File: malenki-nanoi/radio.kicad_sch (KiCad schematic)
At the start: 22 parts, among them U1 A7105, Y1 16 Mhz 20ppm

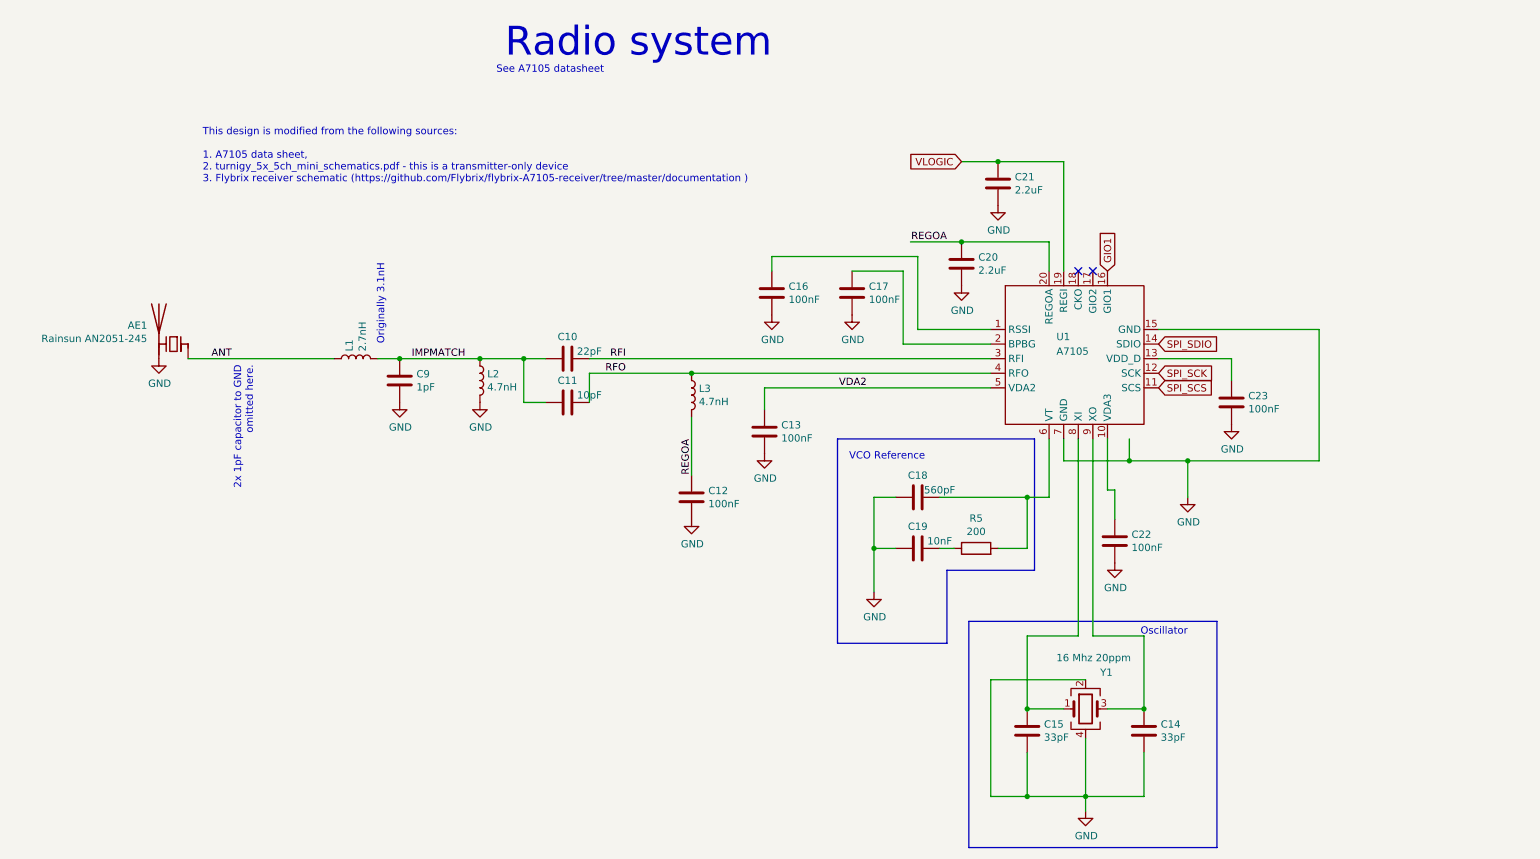
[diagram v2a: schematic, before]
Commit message: 4-layer Malenki-nano
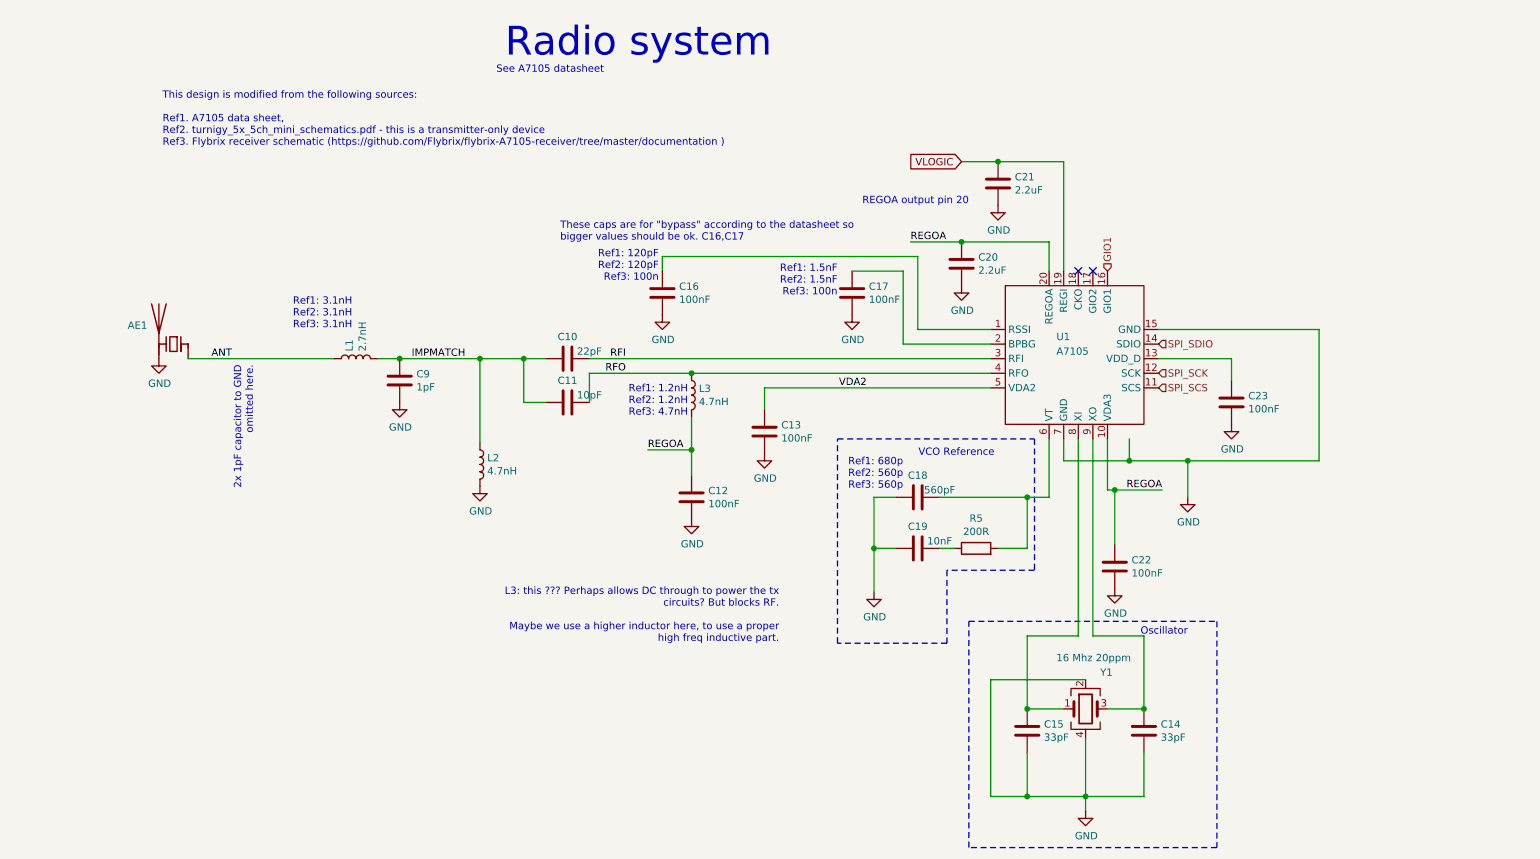
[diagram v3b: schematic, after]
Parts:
- AE1: value Rainsun AN2051-245 -> ~; footprint RF_Antenna:Johanson_2450AT43F0100 -> RF_Antenna:Texas_SWRA117D_2.4GHz_Left; LCSC C99727 -> (none)
- C10: footprint Capacitor_SMD:C_0603_1608Metric -> Capacitor_SMD:C_0402_1005Metric; LCSC C1653 -> (none)
- C11: footprint Capacitor_SMD:C_0603_1608Metric -> Capacitor_SMD:C_0402_1005Metric; LCSC C1634 -> (none)
- C12, C13, C16, C17, C22, C23: footprint Capacitor_SMD:C_0603_1608Metric -> Capacitor_SMD:C_0402_1005Metric; LCSC C14663 -> (none)
- C14, C15: footprint Capacitor_SMD:C_0603_1608Metric -> Capacitor_SMD:C_0402_1005Metric; LCSC C1663 -> (none)
- C18: footprint Capacitor_SMD:C_0603_1608Metric -> Capacitor_SMD:C_0402_1005Metric; LCSC C84721 -> (none)
- C19: footprint Capacitor_SMD:C_0603_1608Metric -> Capacitor_SMD:C_0402_1005Metric; LCSC C57112 -> (none)
- C20, C21: LCSC C23630 -> (none)
- C9: footprint Capacitor_SMD:C_0603_1608Metric -> Capacitor_SMD:C_0402_1005Metric; LCSC C23969 -> (none)
- L1, L2, L3: footprint Inductor_SMD:L_0603_1608Metric -> Inductor_SMD:L_0402_1005Metric
- R5: value 200 -> 200R; footprint Resistor_SMD:R_0603_1608Metric -> Resistor_SMD:R_0402_1005Metric
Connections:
- net REGOA: now also C22.1, U1.10 (VDA3)
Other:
- note added: "L3: this ??? Perhaps allows DC through to power the tx circuits? But blocks RF. Maybe we use a higher inductor here, to use a proper high freq inductive part."
- note added: "REGOA output pin 20"
- note added: "Ref1: 1.2nH Ref2: 1.2nH Ref3: 4.7nH"
- note added: "Ref1: 1.5nF Ref2: 1.5nF Ref3: 100n"
- note added: "Ref1: 120pF Ref2: 120pF Ref3: 100n"
- note added: "Ref1: 3.1nH Ref2: 3.1nH Ref3: 3.1nH"
- note added: "Ref1: 680p Ref2: 560p Ref3: 560p"
- note added: "These caps are for "bypass" according to the datasheet so bigger values should be ok. C16,C17"
- note added: "This design is modified from the following sources: Ref1. A7105 data sheet, Ref2. turnigy_5x_5ch_mini_schematics.pdf - this is a transmitter-only device Ref3. Flybrix receiver schematic (https://github.com/Flybrix/flybrix-A7105-receiver/tree/master/documentation )"
- note removed: "Originally 3.1nH"
- note removed: "This design is modified from the following sources: 1. A7105 data sheet, 2. turnigy_5x_5ch_mini_schematics.pdf - this is a transmitter-only device 3. Flybrix receiver schematic (https://github.com/Flybrix/flybrix-A7105-receiver/tree/master/documentation )"
- moved on the sheet: C16, C22, L2

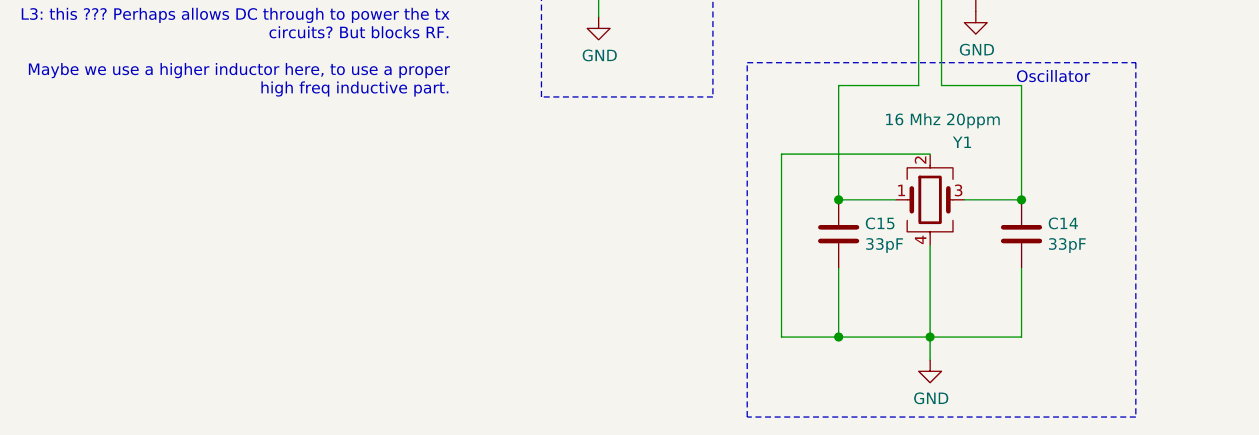
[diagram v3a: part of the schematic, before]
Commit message: Crystal caps update
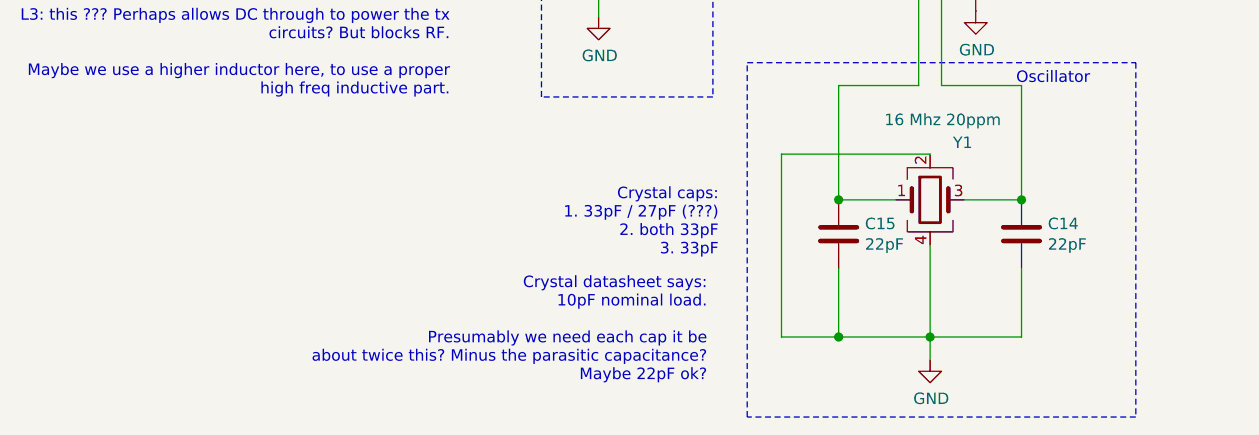
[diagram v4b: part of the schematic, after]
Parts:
- C14, C15: value 33pF -> 22pF
- R5: LCSC C8218 -> (none)
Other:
- note added: "Crystal caps: 1. 33pF / 27pF (???) 2. both 33pF 3. 33pF"
- note added: "Crystal datasheet says: 10pF nominal load. Presumably we need each cap it be about twice this? Minus the parasitic capacitance? Maybe 22pF ok?"
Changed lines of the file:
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@@
+    (effects (font (size 1.27 1.27)) (justify right bottom))
+  )
+  (text "Crystal datasheet says:\n10pF nominal load.\n\nPresumably we need each cap it be\nabout twice this? Minus the parasitic capacitance?\nMaybe 22pF ok?"
+    (at 193.675 157.48 0)
+    (effects (font (size 1.27 1.27)) (justify right bottom))
+  )
+  (text "Crystal caps:\n1. 33pF / 27pF (???)\n2. both 33pF\n3. 33pF"
+    (at 194.945 143.51 0)
     (effects (font (size 1.27 1.27)) (justify right bottom))
   )
@@
       (effects (font (size 1.27 1.27)) hide)
     )
-    (property "LCSC" "C8218" (id 4) (at 199.39 109.22 0)
+    (property "LCSC" "" (id 4) (at 199.39 109.22 0)
       (effects (font (size 1.27 1.27)) hide)
     )
@@
       (effects (font (size 1.27 1.27)) (justify left))
     )
-    (property "Value" "33pF" (id 1) (at 211.201 142.113 0)
+    (property "Value" "22pF" (id 1) (at 211.201 142.113 0)
       (effects (font (size 1.27 1.27)) (justify left))
     )
@@
       (effects (font (size 1.27 1.27)) (justify left))
     )
-    (property "Value" "33pF" (id 1) (at 231.521 142.113 0)
-      (effects (font (size 1.27 1.27)) (justify left))
-    )
+    (property "Value" "22pF" (id 1) (at 231.521 142.113 0)
+      (effects (font (size 1.27 1.27)) (justify left))
+    )

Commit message: Use hand-solder footprints for all 0402
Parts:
- C10, C11, C12, C13, C14, C15, C16, C17, C18, C19, C22, C23, C9: footprint Capacitor_SMD:C_0402_1005Metric -> Capacitor_SMD:C_0402_1005Metric_Pad0.74x0.62mm_HandSolder
- L1, L2, L3: footprint Inductor_SMD:L_0402_1005Metric -> Inductor_SMD:L_0402_1005Metric_Pad0.77x0.64mm_HandSolder
- R5: footprint Resistor_SMD:R_0402_1005Metric -> Resistor_SMD:R_0402_1005Metric_Pad0.72x0.64mm_HandSolder
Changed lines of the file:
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@@
       (effects (font (size 1.27 1.27)) (justify left))
     )
-    (property "Footprint" "Inductor_SMD:L_0402_1005Metric" (id 2) (at 91.44 76.2 0)
+    (property "Footprint" "Inductor_SMD:L_0402_1005Metric_Pad0.77x0.64mm_HandSolder" (id 2) (at 91.44 76.2 0)
       (effects (font (size 1.27 1.27)) hide)
     )
@@
       (effects (font (size 1.27 1.27)) (justify left))
     )
-    (property "Footprint" "Inductor_SMD:L_0402_1005Metric" (id 2) (at 113.03 94.615 0)
+    (property "Footprint" "Inductor_SMD:L_0402_1005Metric_Pad0.77x0.64mm_HandSolder" (id 2) (at 113.03 94.615 0)
       (effects (font (size 1.27 1.27)) hide)
     )
@@
       (effects (font (size 1.27 1.27)) (justify left))
     )
-    (property "Footprint" "Inductor_SMD:L_0402_1005Metric" (id 2) (at 149.86 82.55 0)
+    (property "Footprint" "Inductor_SMD:L_0402_1005Metric_Pad0.77x0.64mm_HandSolder" (id 2) (at 149.86 82.55 0)
       (effects (font (size 1.27 1.27)) hide)
     )
@@
     (property "Reference" "R5" (id 0) (at 199.39 103.9876 90))
     (property "Value" "200R" (id 1) (at 199.39 106.299 90))
-    (property "Footprint" "Resistor_SMD:R_0402_1005Metric" (id 2) (at 199.39 110.998 90)
+    (property "Footprint" "Resistor_SMD:R_0402_1005Metric_Pad0.72x0.64mm_HandSolder" (id 2) (at 199.39 110.998 90)
       (effects (font (size 1.27 1.27)) hide)
     )
@@
       (effects (font (size 1.27 1.27)) (justify left))
     )
-    (property "Footprint" "Capacitor_SMD:C_0402_1005Metric" (id 2) (at 100.0252 83.82 0)
+    (property "Footprint" "Capacitor_SMD:C_0402_1005Metric_Pad0.74x0.62mm_HandSolder" (id 2) (at 100.0252 83.82 0)
       (effects (font (size 1.27 1.27)) hide)
     )
@@
     (property "Reference" "C10" (id 0) (at 128.27 72.39 90))
     (property "Value" "22pF" (id 1) (at 132.08 74.93 90))
-    (property "Footprint" "Capacitor_SMD:C_0402_1005Metric" (id 2) (at 132.08 75.2348 0)
+    (property "Footprint" "Capacitor_SMD:C_0402_1005Metric_Pad0.74x0.62mm_HandSolder" (id 2) (at 132.08 75.2348 0)
       (effects (font (size 1.27 1.27)) hide)
     )
@@
     (property "Reference" "C11" (id 0) (at 128.27 80.01 90))
     (property "Value" "10pF" (id 1) (at 132.08 82.55 90))
-    (property "Footprint" "Capacitor_SMD:C_0402_1005Metric" (id 2) (at 132.08 82.8548 0)
+    (property "Footprint" "Capacitor_SMD:C_0402_1005Metric_Pad0.74x0.62mm_HandSolder" (id 2) (at 132.08 82.8548 0)
       (effects (font (size 1.27 1.27)) hide)
     )
@@
       (effects (font (size 1.27 1.27)) (justify left))
     )
-    (property "Footprint" "Capacitor_SMD:C_0402_1005Metric" (id 2) (at 145.7452 68.58 0)
+    (property "Footprint" "Capacitor_SMD:C_0402_1005Metric_Pad0.74x0.62mm_HandSolder" (id 2) (at 145.7452 68.58 0)
       (effects (font (size 1.27 1.27)) hide)
     )
@@
       (effects (font (size 1.27 1.27)) (justify left))
     )
-    (property "Footprint" "Capacitor_SMD:C_0402_1005Metric" (id 2) (at 150.8252 104.14 0)
+    (property "Footprint" "Capacitor_SMD:C_0402_1005Metric_Pad0.74x0.62mm_HandSolder" (id 2) (at 150.8252 104.14 0)
       (effects (font (size 1.27 1.27)) hide)
     )
@@
       (effects (font (size 1.27 1.27)) (justify left))
     )
-    (property "Footprint" "Capacitor_SMD:C_0402_1005Metric" (id 2) (at 163.5252 92.71 0)
+    (property "Footprint" "Capacitor_SMD:C_0402_1005Metric_Pad0.74x0.62mm_HandSolder" (id 2) (at 163.5252 92.71 0)
       (effects (font (size 1.27 1.27)) hide)
     )
@@
       (effects (font (size 1.27 1.27)) (justify left))
     )
-    (property "Footprint" "Capacitor_SMD:C_0402_1005Metric" (id 2) (at 178.7652 68.58 0)
+    (property "Footprint" "Capacitor_SMD:C_0402_1005Metric_Pad0.74x0.62mm_HandSolder" (id 2) (at 178.7652 68.58 0)
       (effects (font (size 1.27 1.27)) hide)
     )
@@
     (property "Reference" "C18" (id 0) (at 189.23 96.52 90))
     (property "Value" "560pF" (id 1) (at 193.04 99.06 90))
-    (property "Footprint" "Capacitor_SMD:C_0402_1005Metric" (id 2) (at 193.04 99.3648 0)
+    (property "Footprint" "Capacitor_SMD:C_0402_1005Metric_Pad0.74x0.62mm_HandSolder" (id 2) (at 193.04 99.3648 0)
       (effects (font (size 1.27 1.27)) hide)
     )
@@
     (property "Reference" "C19" (id 0) (at 189.23 105.41 90))
     (property "Value" "10nF" (id 1) (at 193.04 107.95 90))
-    (property "Footprint" "Capacitor_SMD:C_0402_1005Metric" (id 2) (at 185.42 110.1852 0)
+    (property "Footprint" "Capacitor_SMD:C_0402_1005Metric_Pad0.74x0.62mm_HandSolder" (id 2) (at 185.42 110.1852 0)
       (effects (font (size 1.27 1.27)) hide)
     )
@@
       (effects (font (size 1.27 1.27)) (justify left))
     )
-    (property "Footprint" "Capacitor_SMD:C_0402_1005Metric" (id 2) (at 209.2452 144.78 0)
+    (property "Footprint" "Capacitor_SMD:C_0402_1005Metric_Pad0.74x0.62mm_HandSolder" (id 2) (at 209.2452 144.78 0)
       (effects (font (size 1.27 1.27)) hide)
     )
@@
       (effects (font (size 1.27 1.27)) (justify left))
     )
-    (property "Footprint" "Capacitor_SMD:C_0402_1005Metric" (id 2) (at 224.4852 116.205 0)
+    (property "Footprint" "Capacitor_SMD:C_0402_1005Metric_Pad0.74x0.62mm_HandSolder" (id 2) (at 224.4852 116.205 0)
       (effects (font (size 1.27 1.27)) hide)
     )
@@
       (effects (font (size 1.27 1.27)) (justify left))
     )
-    (property "Footprint" "Capacitor_SMD:C_0402_1005Metric" (id 2) (at 229.5652 144.78 0)
+    (property "Footprint" "Capacitor_SMD:C_0402_1005Metric_Pad0.74x0.62mm_HandSolder" (id 2) (at 229.5652 144.78 0)
       (effects (font (size 1.27 1.27)) hide)
     )
@@
       (effects (font (size 1.27 1.27)) (justify left))
     )
-    (property "Footprint" "Capacitor_SMD:C_0402_1005Metric" (id 2) (at 244.8052 87.63 0)
-      (effects (font (size 1.27 1.27)) hide)
-    )
+    (property "Footprint" "Capacitor_SMD:C_0402_1005Metric_Pad0.74x0.62mm_HandSolder" (id 2) (at 244.8052 87.63 0)
+      (effects (font (size 1.27 1.27)) hide)
+    )

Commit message: update some comments pin1 marks on silkscreen
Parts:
- Y1: value 16 Mhz 20ppm -> 16 Mhz 20ppm ABM10-16.000MHZ-E20-T
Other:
- note added: "Crystal requirements (from A7105 datasheet) - ESR <= 80ohm Firmware FC on - accuracy 20ppm Firmware FC off - accuracy 10ppm"
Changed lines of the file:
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@@
     (effects (font (size 1.27 1.27)) (justify right bottom))
+  )
+  (text "Crystal requirements (from A7105 datasheet)\n- ESR <= 80ohm\nFirmware FC on - accuracy 20ppm\nFirmware FC off - accuracy 10ppm"
+    (at 242.57 139.7 0)
+    (effects (font (size 1.27 1.27)) (justify left bottom))
   )
   (label "ANT" (at 69.85 76.2 180)
@@
       (effects (font (size 1.27 1.27)) (justify left))
     )
-    (property "Value" "16 Mhz 20ppm" (id 1) (at 213.36 128.27 0)
+    (property "Value" "16 Mhz 20ppm ABM10-16.000MHZ-E20-T " (id 1) (at 213.36 128.27 0)
       (effects (font (size 1.27 1.27)) (justify left))
     )
@@
       (effects (font (size 1.27 1.27)) hide)
     )
-    (property "Datasheet" "~" (id 3) (at 218.44 137.16 0)
-      (effects (font (size 1.27 1.27)) hide)
-    )
+    (property "Datasheet" "https://datasheet.lcsc.com/szlcsc/1810170922_Abracon-LLC-ABM10-16-000MHZ-E20-T_C179632.pdf" (id 3) (at 218.44 137.16 0)
+      (effects (font (size 1.27 1.27)) hide)
+    )
